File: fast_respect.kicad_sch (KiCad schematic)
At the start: 16 parts, among them J1_1 Conn_02x04_Odd_Even, SW1_1 SW_Push, SW1_2 SW_Push, U1_1 STM32F446RETx

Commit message: VCAP1のコンデンサの値追加
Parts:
- C1_10: value C -> 4.7uF
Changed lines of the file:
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@@
       (effects (font (size 1.27 1.27)) (justify left))
     )
-    (property "Value" "C" (at 113.03 142.24 0)
+    (property "Value" "4.7uF" (at 113.03 142.24 0)
       (effects (font (size 1.27 1.27)) (justify left))
     )

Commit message: アノテーション番号ミスの修正とフットプリント割り当て途中（部品リストも途中生成）
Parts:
- C1_1, C1_10, C1_2, C1_3, C1_4, C1_5, C1_6, C1_7, C1_8, C1_9: footprint (none) -> Capacitor_SMD:C_0603_1608Metric_Pad1.08x0.95mm_HandSolder
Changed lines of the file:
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@@
       (effects (font (size 1.27 1.27)) (justify left))
     )
-    (property "Footprint" "" (at 150.8252 60.96 0)
+    (property "Footprint" "Capacitor_SMD:C_0603_1608Metric_Pad1.08x0.95mm_HandSolder" (at 150.8252 60.96 0)
       (effects (font (size 1.27 1.27)) hide)
     )
@@
       (effects (font (size 1.27 1.27)) (justify left))
     )
-    (property "Footprint" "" (at 129.2352 50.8 0)
+    (property "Footprint" "Capacitor_SMD:C_0603_1608Metric_Pad1.08x0.95mm_HandSolder" (at 129.2352 50.8 0)
       (effects (font (size 1.27 1.27)) hide)
     )
@@
       (effects (font (size 1.27 1.27)) (justify left))
     )
-    (property "Footprint" "" (at 112.7252 59.69 0)
+    (property "Footprint" "Capacitor_SMD:C_0603_1608Metric_Pad1.08x0.95mm_HandSolder" (at 112.7252 59.69 0)
       (effects (font (size 1.27 1.27)) hide)
     )
@@
       (effects (font (size 1.27 1.27)) (justify left))
     )
-    (property "Footprint" "" (at 144.4752 60.96 0)
+    (property "Footprint" "Capacitor_SMD:C_0603_1608Metric_Pad1.08x0.95mm_HandSolder" (at 144.4752 60.96 0)
       (effects (font (size 1.27 1.27)) hide)
     )
@@
       (effects (font (size 1.27 1.27)) (justify left))
     )
-    (property "Footprint" "" (at 157.1752 60.96 0)
+    (property "Footprint" "Capacitor_SMD:C_0603_1608Metric_Pad1.08x0.95mm_HandSolder" (at 157.1752 60.96 0)
       (effects (font (size 1.27 1.27)) hide)
     )
@@
       (effects (font (size 1.27 1.27)) (justify left))
     )
-    (property "Footprint" "" (at 122.8852 50.8 0)
+    (property "Footprint" "Capacitor_SMD:C_0603_1608Metric_Pad1.08x0.95mm_HandSolder" (at 122.8852 50.8 0)
       (effects (font (size 1.27 1.27)) hide)
     )
@@
       (effects (font (size 1.27 1.27)) (justify left))
     )
-    (property "Footprint" "" (at 141.9352 50.8 0)
+    (property "Footprint" "Capacitor_SMD:C_0603_1608Metric_Pad1.08x0.95mm_HandSolder" (at 141.9352 50.8 0)
       (effects (font (size 1.27 1.27)) hide)
     )
@@
       (effects (font (size 1.27 1.27)) (justify left))
     )
-    (property "Footprint" "" (at 65.7352 44.45 0)
+    (property "Footprint" "Capacitor_SMD:C_0603_1608Metric_Pad1.08x0.95mm_HandSolder" (at 65.7352 44.45 0)
       (effects (font (size 1.27 1.27)) hide)
     )
@@
       (effects (font (size 1.27 1.27)) (justify left))
     )
-    (property "Footprint" "" (at 135.5852 50.8 0)
+    (property "Footprint" "Capacitor_SMD:C_0603_1608Metric_Pad1.08x0.95mm_HandSolder" (at 135.5852 50.8 0)
       (effects (font (size 1.27 1.27)) hide)
     )
@@
       (effects (font (size 1.27 1.27)) (justify left))
     )
-    (property "Footprint" "" (at 110.1852 144.78 0)
-      (effects (font (size 1.27 1.27)) hide)
-    )
+    (property "Footprint" "Capacitor_SMD:C_0603_1608Metric_Pad1.08x0.95mm_HandSolder" (at 110.1852 144.78 0)
+      (effects (font (size 1.27 1.27)) hide)
+    )

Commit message: フェライトビーズに型番追加し、自作パッケージの構成へこう
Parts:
- FB1_1: footprint (none) -> Resistor_SMD:R_0603_1608Metric
- R1_1: footprint (none) -> Resistor_SMD:R_0603_1608Metric_Pad0.98x0.95mm_HandSolder
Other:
- note added: "MZ1608-102Y"
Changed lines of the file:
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@@
+    (effects (font (size 1.27 1.27)) (justify left bottom))
+  )
+  (text "MZ1608-102Y" (at 154.94 34.29 0)
     (effects (font (size 1.27 1.27)) (justify left bottom))
   )
@@
   )
   (symbol (lib_id "Device:FerriteBead") (at 161.29 44.45 270) (unit 1)
-    (in_bom yes) (on_board yes) (dnp no) (fields_autoplaced)
+    (in_bom yes) (on_board yes) (dnp no)
     (property "Reference" "FB1_1" (at 161.3408 36.83 90)
       (effects (font (size 1.27 1.27)))
@@
       (effects (font (size 1.27 1.27)))
     )
-    (property "Footprint" "" (at 161.29 42.672 90)
+    (property "Footprint" "Resistor_SMD:R_0603_1608Metric" (at 161.29 42.672 90)
       (effects (font (size 1.27 1.27)) hide)
     )
@@
       (effects (font (size 1.27 1.27)) (justify left))
     )
-    (property "Footprint" "" (at 23.622 46.99 90)
-      (effects (font (size 1.27 1.27)) hide)
-    )
+    (property "Footprint" "Resistor_SMD:R_0603_1608Metric_Pad0.98x0.95mm_HandSolder" (at 23.622 46.99 90)
+      (effects (font (size 1.27 1.27)) hide)
+    )

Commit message: スイッチ以外のフットプリント割当完了
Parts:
- J1_1: footprint (none) -> Connector_PinHeader_2.54mm:PinHeader_2x04_P2.54mm_Vertical
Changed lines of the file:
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@@
       (effects (font (size 1.27 1.27)))
     )
-    (property "Footprint" "" (at 52.07 81.28 0)
+    (property "Footprint" "Connector_PinHeader_2.54mm:PinHeader_2x04_P2.54mm_Vertical" (at 52.07 81.28 0)
       (effects (font (size 1.27 1.27)) hide)
     )

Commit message: 秋月電子のスライドスイッチのフットプリントを追加して全てのフットプリント割当も完了
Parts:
- SW1_1, SW1_2: footprint (none) -> Button_Switch_THT:SW_PUSH_6mm
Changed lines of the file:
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@@
       (effects (font (size 1.27 1.27)) (justify left))
     )
-    (property "Footprint" "" (at 50.8 40.64 0)
+    (property "Footprint" "Button_Switch_THT:SW_PUSH_6mm" (at 50.8 40.64 0)
       (effects (font (size 1.27 1.27)) hide)
     )
@@
       (effects (font (size 1.27 1.27)) (justify left))
     )
-    (property "Footprint" "" (at 30.48 33.02 0)
+    (property "Footprint" "Button_Switch_THT:SW_PUSH_6mm" (at 30.48 33.02 0)
       (effects (font (size 1.27 1.27)) hide)
     )

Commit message: 吸引ファンのシートとピン追加
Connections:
- net FAN_MOTOR_PWM: now reaches U1_1.61 (PB8)
- net FAN_MOTOR_PHASE: now reaches U1_1.62 (PB9)
- no-connect marks 19 -> 17
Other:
- sheet Power renamed POWER
- added sheet SUCTION FAN (suction_fan.kicad_sch)
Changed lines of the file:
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@@
   (no_connect (at 153.67 72.39))
   (no_connect (at 153.67 100.33))
-  (no_connect (at 153.67 133.35))
-  (no_connect (at 153.67 135.89))
   (no_connect (at 118.11 80.01))
   (no_connect (at 118.11 87.63))
@@
     (stroke (width 0) (type default))
   )
+  (wire (pts (xy 203.2 138.43) (xy 204.47 138.43))
+    (stroke (width 0) (type default))
+  )
   (wire (pts (xy 138.43 60.96) (xy 140.97 60.96))
     (stroke (width 0) (type default))
@@
   )
   (wire (pts (xy 45.72 33.02) (xy 64.77 33.02))
+    (stroke (width 0) (type default))
+  )
+  (wire (pts (xy 203.2 134.62) (xy 204.47 134.62))
     (stroke (width 0) (type default))
   )
@@
     )
   )
+  (global_label "FAN_MOTOR_PHASE" (shape input) (at 203.2 138.43 180) (fields_autoplaced)
+    (effects (font (size 1.27 1.27)) (justify right))
+    (property "Intersheetrefs" "${INTERSHEET_REFS}" (at 182.3743 138.43 0)
+      (effects (font (size 1.27 1.27)) (justify right) hide)
+    )
+  )
   (global_label "NRST" (shape output) (at 74.93 33.02 0) (fields_autoplaced)
     (effects (font (size 1.27 1.27)) (justify left))
@@
     )
   )
+  (global_label "FAN_MOTOR_PHASE" (shape output) (at 153.67 135.89 0) (fields_autoplaced)
+    (effects (font (size 1.27 1.27)) (justify left))
+    (property "Intersheetrefs" "${INTERSHEET_REFS}" (at 174.4957 135.89 0)
+      (effects (font (size 1.27 1.27)) (justify left) hide)
+    )
+  )
   (global_label "GYRO_MISO" (shape input) (at 153.67 146.05 0) (fields_autoplaced)
     (effects (font (size 1.27 1.27)) (justify left))
@@
     )
   )
+  (global_label "FAN_MOTOR_PWM" (shape input) (at 203.2 134.62 180) (fields_autoplaced)
+    (effects (font (size 1.27 1.27)) (justify right))
+    (property "Intersheetrefs" "${INTERSHEET_REFS}" (at 184.2491 134.62 0)
+      (effects (font (size 1.27 1.27)) (justify right) hide)
+    )
+  )
   (global_label "SWO" (shape input) (at 153.67 120.65 0) (fields_autoplaced)
     (effects (font (size 1.27 1.27)) (justify left))
@@
     (effects (font (size 1.27 1.27)) (justify left))
     (property "Intersheetrefs" "${INTERSHEET_REFS}" (at 39.5733 40.64 0)
+      (effects (font (size 1.27 1.27)) (justify left) hide)
+    )
+  )
+  (global_label "FAN_MOTOR_PWM" (shape output) (at 153.67 133.35 0) (fields_autoplaced)
+    (effects (font (size 1.27 1.27)) (justify left))
+    (property "Intersheetrefs" "${INTERSHEET_REFS}" (at 172.6209 133.35 0)
       (effects (font (size 1.27 1.27)) (justify left) hide)
     )
@@
     (stroke (width 0.1524) (type solid))
     (fill (color 0 0 0 0.0000))
-    (property "Sheetname" "Power" (at 38.1 104.6984 0)
+    (property "Sheetname" "POWER" (at 38.1 104.6984 0)
       (effects (font (size 1.27 1.27)) (justify left bottom))
     )
@@
       )
     )
+  )
+  (sheet (at 204.47 130.81) (size 20.32 11.43) (fields_autoplaced)
+    (stroke (width 0.1524) (type solid))
+    (fill (color 0 0 0 0.0000))
+    (property "Sheetname" "SUCTION FAN" (at 204.47 130.0984 0)
+      (effects (font (size 1.27 1.27)) (justify left bottom))
+    )
+    (property "Sheetfile" "suction_fan.kicad_sch" (at 204.47 142.8246 0)
+      (effects (font (size 1.27 1.27)) (justify left top))
+    )
+    (pin "FAN_MOTOR_PHASE" input (at 204.47 138.43 180)
+      (effects (font (size 1.27 1.27)) (justify left))
+    )
+    (pin "FAN_MOTOR_PWM" input (at 204.47 134.62 180)
+      (effects (font (size 1.27 1.27)) (justify left))
+    )
+    (instances
+      (project "fast_respect"
+        (path "/588ca8cd-b11b-4b55-96d9-278aac6cd0cf" (page "7"))
+      )
+    )

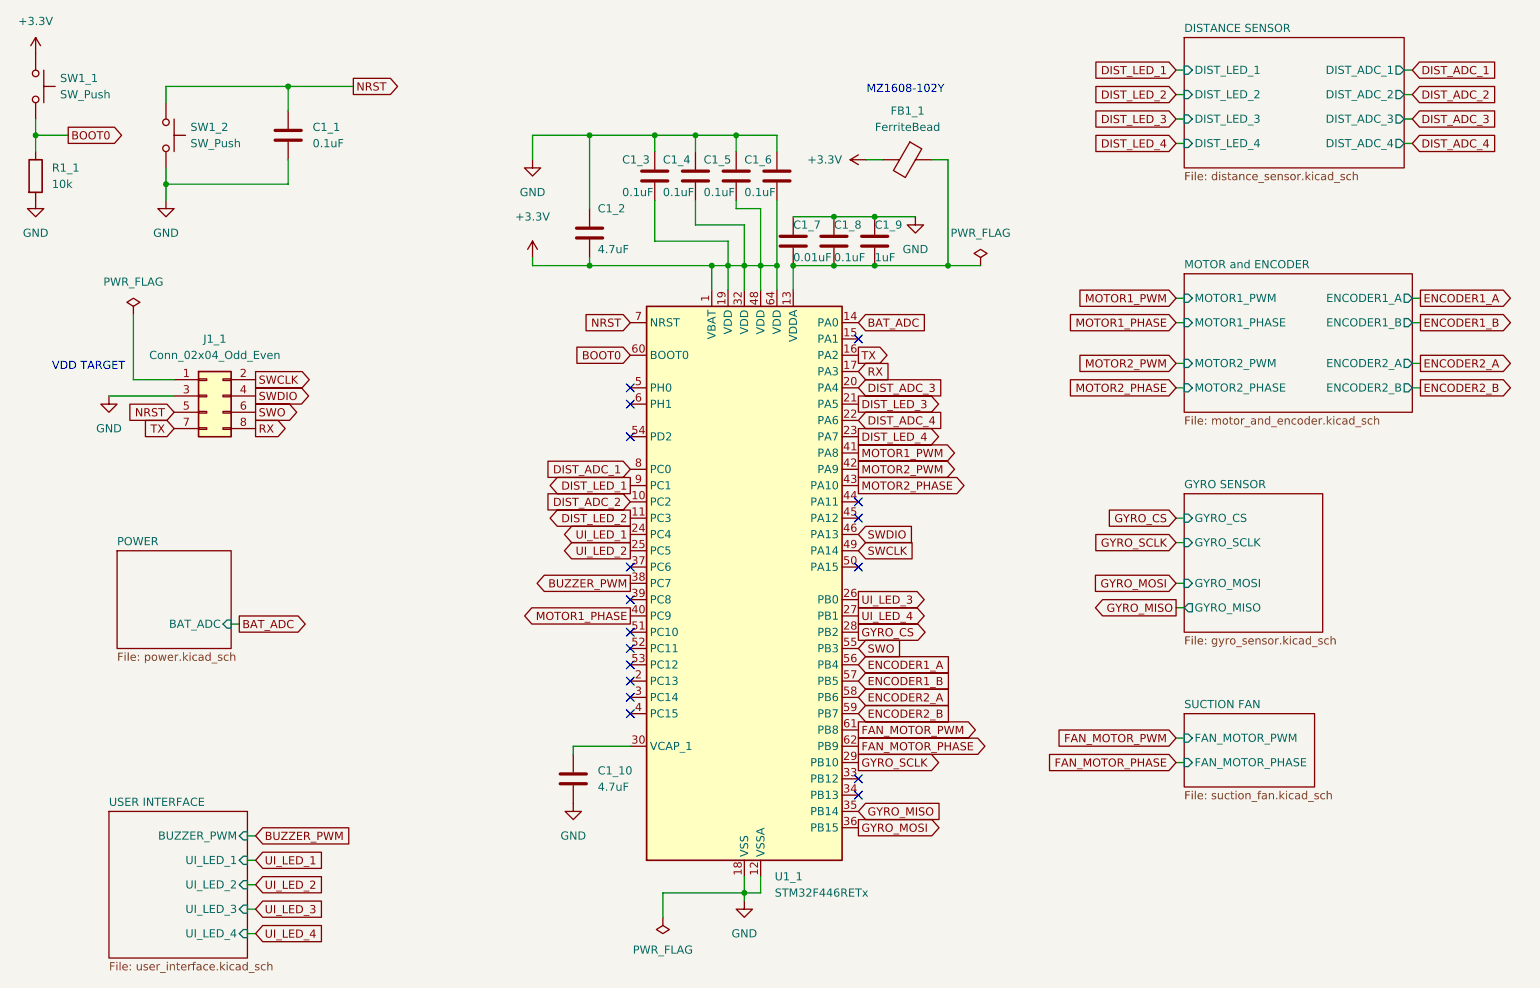
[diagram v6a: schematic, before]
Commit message: 吸引モータ周りの回路修正
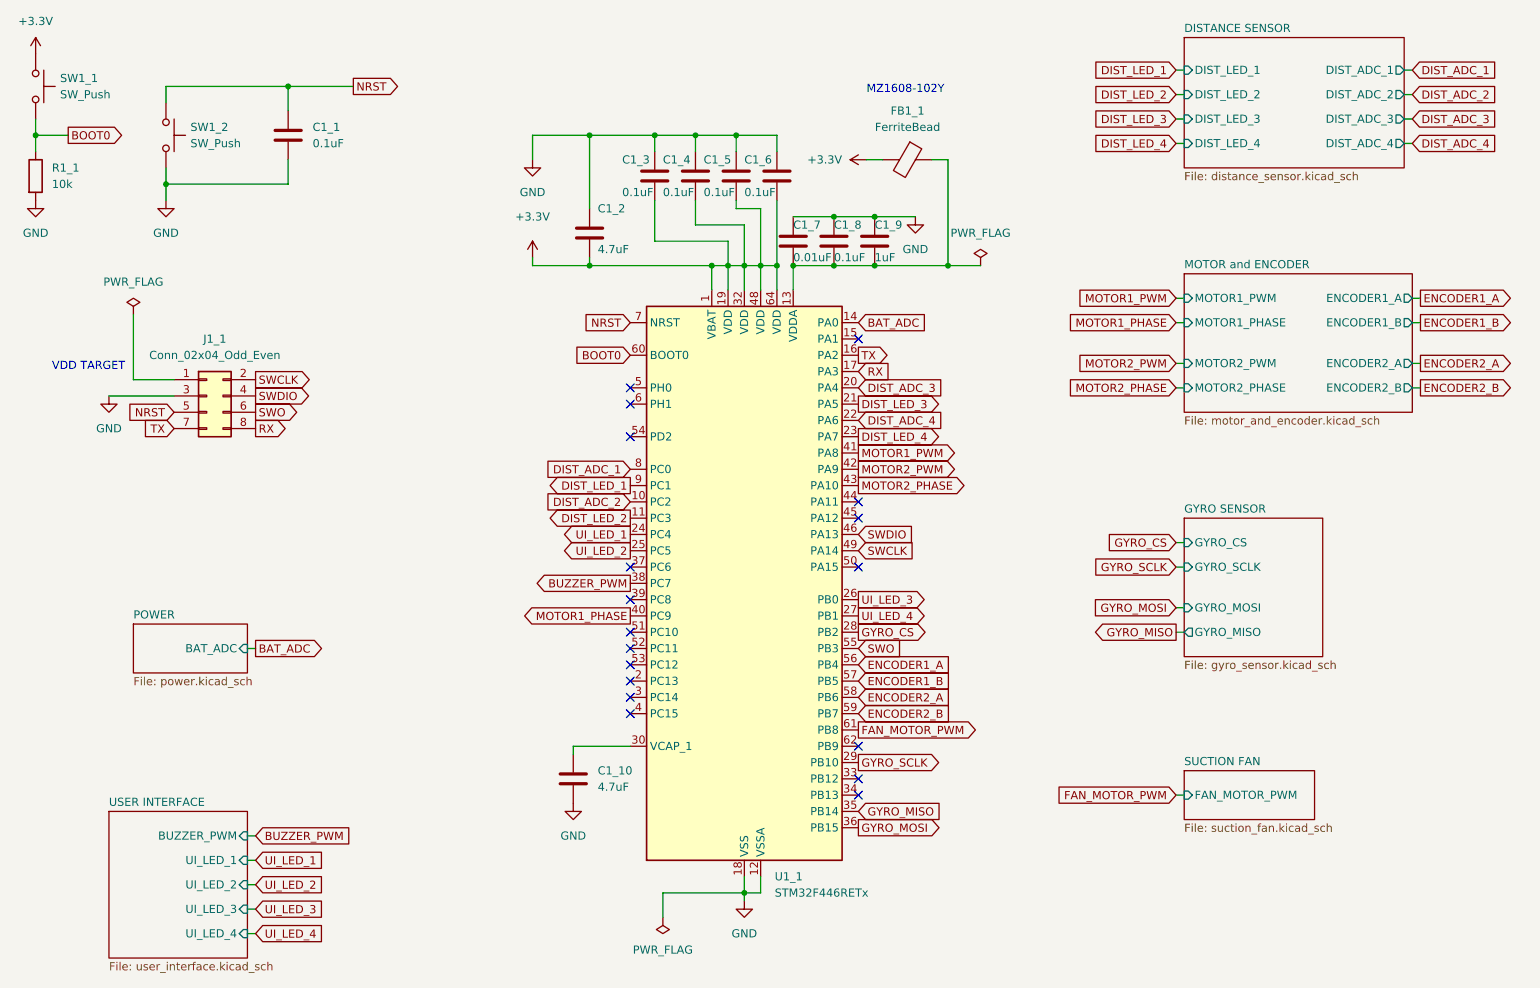
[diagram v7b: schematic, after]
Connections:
- net FAN_MOTOR_PHASE: no longer names the net of U1_1.62 (PB9)
- no-connect marks 17 -> 18
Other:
- sheet SUCTION FAN ports: added none; removed FAN_MOTOR_PHASE

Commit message: 押しボタンスイッチのフットプリント割り当てを変更
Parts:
- SW1_1, SW1_2: footprint Button_Switch_THT:SW_PUSH_6mm -> Button_Switch_SMD:SW_Push_1P1T_NO_Vertical_Wuerth_434133025816
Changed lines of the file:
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@@
       (effects (font (size 1.27 1.27)) (justify left))
     )
-    (property "Footprint" "Button_Switch_THT:SW_PUSH_6mm" (at 50.8 40.64 0)
+    (property "Footprint" "Button_Switch_SMD:SW_Push_1P1T_NO_Vertical_Wuerth_434133025816" (at 50.8 40.64 0)
       (effects (font (size 1.27 1.27)) hide)
     )
@@
       (effects (font (size 1.27 1.27)) (justify left))
     )
-    (property "Footprint" "Button_Switch_THT:SW_PUSH_6mm" (at 30.48 33.02 0)
+    (property "Footprint" "Button_Switch_SMD:SW_Push_1P1T_NO_Vertical_Wuerth_434133025816" (at 30.48 33.02 0)
       (effects (font (size 1.27 1.27)) hide)
     )
